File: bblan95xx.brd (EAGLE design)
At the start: 50 x 50 mm, 49 parts, among them IC1 LAN9512, IC2 93ST, Q1 25MHz

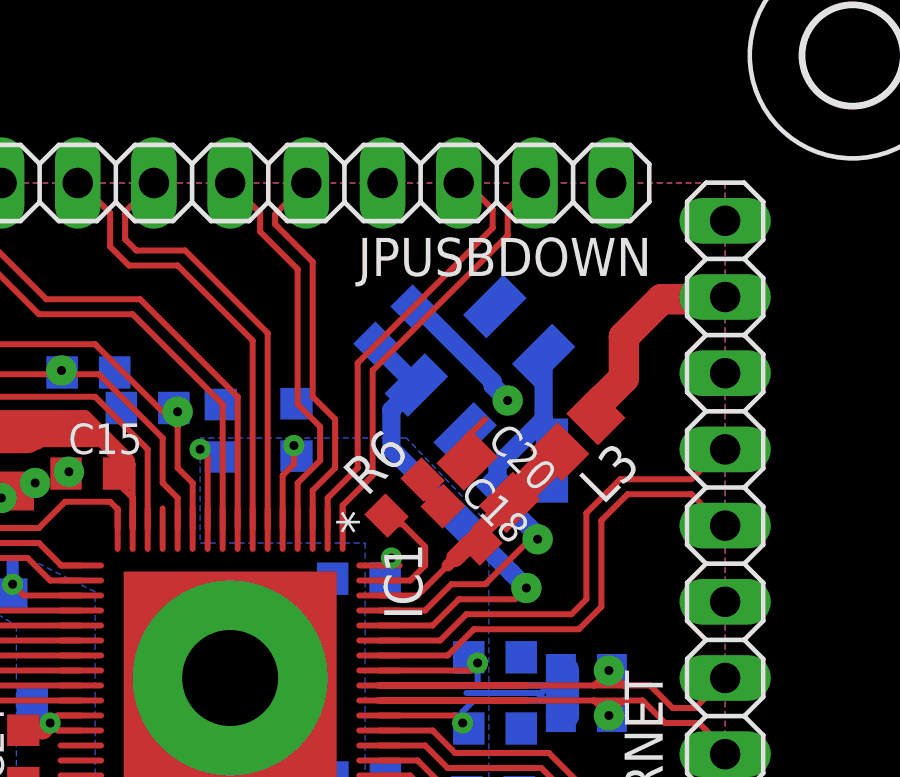
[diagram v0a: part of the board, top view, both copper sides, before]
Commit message: reroute USB down-port two and crystal cap
Signed-off-by: Stephan Baerwolf <stephan@matrixstorm.com>
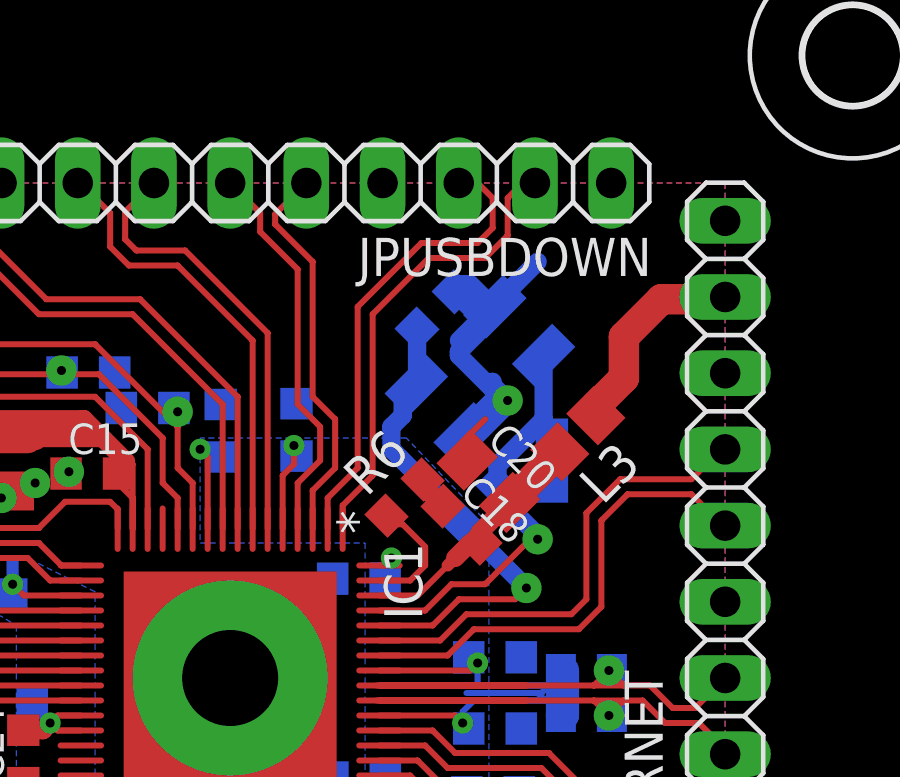
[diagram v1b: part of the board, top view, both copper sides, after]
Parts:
- moved C23 1.46 mm to (31.8, 37.3)
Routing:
- net GND: track 28.6 -> 37.0 mm
- net USBDP2: track 14.4 -> 15.7 mm
- net USBDM2: track 14.2 -> 15.5 mm
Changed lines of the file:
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@@
 <wire x1="29.375" y1="20.625" x2="20.625" y2="20.625" width="1.016" layer="41"/>
 <wire x1="20.625" y1="20.625" x2="20.625" y2="29.375" width="1.016" layer="41"/>
-<wire x1="28.5" y1="29.25" x2="28.5" y2="30.875" width="3" layer="41"/>
-<wire x1="28.5" y1="30.875" x2="29.5" y2="31.875" width="3" layer="41"/>
-<wire x1="29.5" y1="31.875" x2="29.5" y2="35.375" width="3" layer="41"/>
-<wire x1="29.5" y1="35.375" x2="33.875" y2="39.75" width="3" layer="41"/>
-<wire x1="33.875" y1="39.75" x2="33.875" y2="40.75" width="3" layer="41"/>
+<wire x1="28.5" y1="29.25" x2="28.5" y2="30.875" width="2.1844" layer="41"/>
+<wire x1="28.5" y1="30.875" x2="29.5" y2="31.875" width="2.1844" layer="41"/>
+<wire x1="29.5" y1="31.875" x2="29.5" y2="37.25" width="2.1844" layer="41"/>
 <wire x1="27.5" y1="29.25" x2="27.5" y2="31.375" width="3" layer="41"/>
 <wire x1="27.5" y1="31.375" x2="28.125" y2="32" width="3" layer="41"/>
@@
 <wire x1="21.25" y1="39.5" x2="21.25" y2="40.75" width="3" layer="41"/>
 <wire x1="25" y1="29.125" x2="25" y2="34.25" width="3" layer="41"/>
-<wire x1="25" y1="34.25" x2="21.875" y2="37.375" width="3" layer="41"/>
-<wire x1="21.875" y1="37.375" x2="18.75" y2="37.375" width="3" layer="41"/>
-<wire x1="18.75" y1="37.375" x2="16.125" y2="40" width="3" layer="41"/>
+<wire x1="25" y1="34.25" x2="21.875" y2="37.375" width="2.1844" layer="41"/>
+<wire x1="21.875" y1="37.375" x2="18.75" y2="37.375" width="2.1844" layer="41"/>
+<wire x1="18.75" y1="37.375" x2="16.125" y2="40" width="2.1844" layer="41"/>
 <wire x1="16.125" y1="40" x2="16.125" y2="40.75" width="3" layer="41"/>
 <wire x1="29.125" y1="26" x2="32.125" y2="26" width="3" layer="41"/>
@@
 <wire x1="39.875" y1="16.125" x2="41.25" y2="16.125" width="3" layer="41"/>
 <wire x1="40.25" y1="17" x2="40.25" y2="15.25" width="3" layer="41"/>
+<wire x1="29.5" y1="37.25" x2="31.5" y2="39.25" width="2.1844" layer="41"/>
+<wire x1="31.5" y1="39.25" x2="33.375" y2="39.25" width="2.1844" layer="41"/>
+<wire x1="33.375" y1="39.25" x2="34" y2="39.875" width="2.1844" layer="41"/>
+<wire x1="34" y1="39.875" x2="34" y2="41" width="3" layer="41"/>
 </plain>
 <attributes>
@@
 <attribute name="NAME" x="16.73" y="23.51" size="1.016" layer="26" rot="MR180"/>
 </element>
-<element name="C23" library="resistor" package="C0603K" value="33p" x="30.473765625" y="36.752046875" rot="MR315">
-<attribute name="SPICEPREFIX" value="C" x="30.473765625" y="36.752046875" size="1.778" layer="28" rot="MR315" display="off"/>
+<element name="C23" library="resistor" package="C0603K" value="33p" x="31.848765625" y="37.252046875" rot="MR315">
+<attribute name="SPICEPREFIX" value="C" x="31.848765625" y="37.252046875" size="1.778" layer="28" rot="MR315" display="off"/>
 </element>
 <element name="C24" library="resistor" package="C0603K" value=".1u" x="18.105" y="22.385" smashed="yes" rot="R90">
@@
 <vertex x="8.5" y="8.5"/>
 </polygon>
-<wire x1="31.092484375" y1="37.3707625" x2="31.2542375" y2="37.3707625" width="0.6096" layer="16"/>
 <wire x1="31.414678125" y1="31.61518125" x2="31.414678125" y2="31.40854375" width="0.6096" layer="1"/>
 <wire x1="31.414678125" y1="31.40854375" x2="32.094671875" y2="30.72855" width="0.6096" layer="1"/>
-<wire x1="31.2542375" y1="37.3707625" x2="33.75" y2="34.875" width="0.6096" layer="16"/>
 <wire x1="33.75" y1="34.875" x2="33.75" y2="34.75" width="0.6096" layer="16"/>
-<wire x1="33.75" y1="34.75" x2="34.25" y2="34.25" width="0.6096" layer="16"/>
+<wire x1="33.75" y1="34.75" x2="34" y2="34.5" width="0.6096" layer="16"/>
 <contactref element="C19" pad="1"/>
+<wire x1="34" y1="34.5" x2="34.25" y2="34.25" width="0.6096" layer="16"/>
 <wire x1="31.720228125" y1="18.428496875" x2="32.351359375" y2="18.428496875" width="1.016" layer="1"/>
 <wire x1="32.351359375" y1="18.428496875" x2="33.170725" y2="17.60913125" width="1.016" layer="1"/>
@@
 <wire x1="32.900215625" y1="32.264928125" x2="32.900215625" y2="33.025215625" width="0.2" layer="1"/>
 <wire x1="32.900215625" y1="33.025215625" x2="33.5" y2="33.625" width="0.2" layer="1"/>
+<wire x1="32.467484375" y1="37.8707625" x2="33.5" y2="36.838246875" width="0.6096" layer="16"/>
+<wire x1="33.5" y1="36.838246875" x2="33.5" y2="36.75" width="0.6096" layer="16"/>
+<wire x1="33.5" y1="36.75" x2="32.625" y2="35.875" width="0.6096" layer="16"/>
+<wire x1="32.625" y1="35.875" x2="32.625" y2="35.75" width="0.6096" layer="16"/>
+<wire x1="32.625" y1="35.75" x2="34.25" y2="34.125" width="0.6096" layer="16"/>
+<wire x1="34.25" y1="34.125" x2="33" y2="32.875" width="0.6096" layer="16"/>
+<wire x1="33.25" y1="33.75" x2="34" y2="34.5" width="0.6096" layer="16"/>
+<wire x1="35.25" y1="38.875" x2="34.125" y2="37.75" width="0.6096" layer="16"/>
+<wire x1="33" y1="38.125" x2="33.5" y2="37.625" width="0.6096" layer="16"/>
+<wire x1="33" y1="38.125" x2="32.721721875" y2="38.125" width="0.6096" layer="16"/>
+<wire x1="32.721721875" y1="38.125" x2="32.467484375" y2="37.8707625" width="0.6096" layer="16"/>
+<wire x1="32.625" y1="36.25" x2="33.375" y2="37" width="0.6096" layer="16"/>
 </signal>
 <signal name="VDD18CORE">
@@
 <contactref element="C23" pad="2"/>
 <contactref element="Q1" pad="1"/>
-<wire x1="29.85505" y1="36.133328125" x2="29.85505" y2="36.1157875" width="0.6096" layer="16"/>
-<wire x1="29.85505" y1="36.1157875" x2="31.20669375" y2="34.76414375" width="0.6096" layer="16"/>
-<wire x1="31.20669375" y1="34.76414375" x2="30.375" y2="33.93245" width="0.6096" layer="16"/>
-<wire x1="30.375" y1="33.93245" x2="30.375" y2="32.625" width="0.6096" layer="16"/>
 <wire x1="30.375" y1="32.625" x2="32.70859375" y2="30.29140625" width="0.6096" layer="16"/>
 <wire x1="32.70859375" y1="30.29140625" x2="32.70859375" y2="30.178265625" width="0.6096" layer="16"/>
 <wire x1="32.70859375" y1="30.178265625" x2="32.70859375" y2="29.66640625" width="0.2" layer="16"/>
 <via x="34.875" y="28" extent="1-16" drill="0.3" diameter="1.016" shape="octagon"/>
-<wire x1="34.375" y1="28.511859375" x2="34.130928125" y2="28.75593125" width="0.6096" layer="16"/>
 <contactref element="IC1" pad="60"/>
-<wire x1="34.130928125" y1="28.75593125" x2="32.70859375" y2="30.178265625" width="0.6096" layer="16"/>
+<wire x1="34.875" y1="28.011859375" x2="32.70859375" y2="30.178265625" width="0.6096" layer="16"/>
 <wire x1="29.977" y1="26.75" x2="31.75" y2="26.75" width="0.2" layer="1"/>
 <wire x1="31.75" y1="26.75" x2="32.625" y2="27.625" width="0.2" layer="1"/>
@@
 <wire x1="34.5" y1="27.625" x2="34.875" y2="28" width="0.2" layer="1"/>
 <wire x1="34.875" y1="28" x2="34.875" y2="28.011859375" width="0.6096" layer="16"/>
-<wire x1="34.875" y1="28.011859375" x2="34.375" y2="28.511859375" width="0.6096" layer="16"/>
+<wire x1="31.20669375" y1="34.76414375" x2="31.23005" y2="34.7875" width="0.6096" layer="16"/>
+<wire x1="31.23005" y1="34.7875" x2="31.23005" y2="36.633328125" width="0.6096" layer="16"/>
+<wire x1="30.375" y1="32.625" x2="30.375" y2="33.375" width="0.6096" layer="16"/>
+<wire x1="30.375" y1="33.375" x2="30.75" y2="33.75" width="0.6096" layer="16"/>
+<wire x1="30.75" y1="33.75" x2="30.75" y2="34.30745" width="0.6096" layer="16"/>
+<wire x1="30.75" y1="34.30745" x2="31.20669375" y2="34.76414375" width="0.6096" layer="16"/>
 </signal>
 <signal name="EECS">
@@
 <wire x1="28.75" y1="29.977" x2="28.75" y2="30.75" width="0.2" layer="1"/>
 <wire x1="28.75" y1="30.75" x2="29.75" y2="31.75" width="0.2" layer="1"/>
-<wire x1="29.75" y1="31.75" x2="29.75" y2="35.25" width="0.2" layer="1"/>
-<wire x1="29.75" y1="35.25" x2="34.25" y2="39.75" width="0.2" layer="1"/>
-<wire x1="34.25" y1="39.75" x2="34.25" y2="40.625" width="0.2" layer="1"/>
-<wire x1="34.25" y1="40.625" x2="34.75" y2="41.125" width="0.2" layer="1"/>
-<wire x1="35.16" y1="41.5" x2="34.785" y2="41.125" width="0.2" layer="1"/>
-<wire x1="34.785" y1="41.125" x2="34.75" y2="41.125" width="0.2" layer="1"/>
+<wire x1="29.75" y1="31.75" x2="29.75" y2="37.125" width="0.2" layer="1"/>
+<wire x1="29.75" y1="37.125" x2="31.625" y2="39" width="0.2" layer="1"/>
+<wire x1="31.625" y1="39" x2="33.5" y2="39" width="0.2" layer="1"/>
+<wire x1="33.5" y1="39" x2="34.25" y2="39.75" width="0.2" layer="1"/>
+<wire x1="34.25" y1="41" x2="34.25" y2="39.75" width="0.2" layer="1"/>
+<wire x1="34.25" y1="41" x2="34.75" y2="41.5" width="0.2" layer="1"/>
+<wire x1="34.75" y1="41.5" x2="35.16" y2="41.5" width="0.2" layer="1"/>
 </signal>
 <signal name="USBDP2">
@@
 <wire x1="28.25" y1="29.977" x2="28.25" y2="31" width="0.2" layer="1"/>
 <wire x1="28.25" y1="31" x2="29.25" y2="32" width="0.2" layer="1"/>
-<wire x1="29.25" y1="32" x2="29.25" y2="35.5" width="0.2" layer="1"/>
-<wire x1="29.25" y1="35.5" x2="33.75" y2="40" width="0.2" layer="1"/>
-<wire x1="33.75" y1="40.625" x2="33.75" y2="40" width="0.2" layer="1"/>
-<wire x1="33.75" y1="40.625" x2="33.25" y2="41.125" width="0.2" layer="1"/>
-<wire x1="32.62" y1="41.5" x2="32.995" y2="41.125" width="0.2" layer="1"/>
-<wire x1="32.995" y1="41.125" x2="33.25" y2="41.125" width="0.2" layer="1"/>
+<wire x1="29.25" y1="37.375" x2="29.25" y2="32" width="0.2" layer="1"/>
+<wire x1="29.25" y1="37.375" x2="31.375" y2="39.5" width="0.2" layer="1"/>
+<wire x1="31.375" y1="39.5" x2="33.25" y2="39.5" width="0.2" layer="1"/>
+<wire x1="33.25" y1="39.5" x2="33.75" y2="40" width="0.2" layer="1"/>
+<wire x1="33.75" y1="40" x2="33.75" y2="41" width="0.2" layer="1"/>
+<wire x1="33.75" y1="41" x2="33.25" y2="41.5" width="0.2" layer="1"/>
+<wire x1="33.25" y1="41.5" x2="32.62" y2="41.5" width="0.2" layer="1"/>
 </signal>
 <signal name="USBDM3">

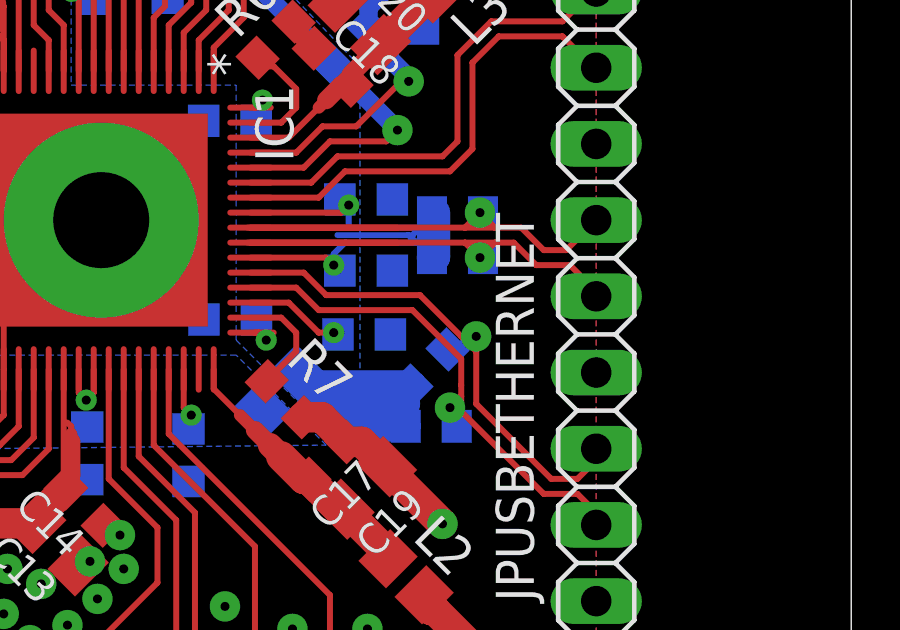
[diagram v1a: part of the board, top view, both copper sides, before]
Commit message: add extra analog capacitor and route VDD33A to free PIN
Signed-off-by: Stephan Baerwolf <stephan@matrixstorm.com>
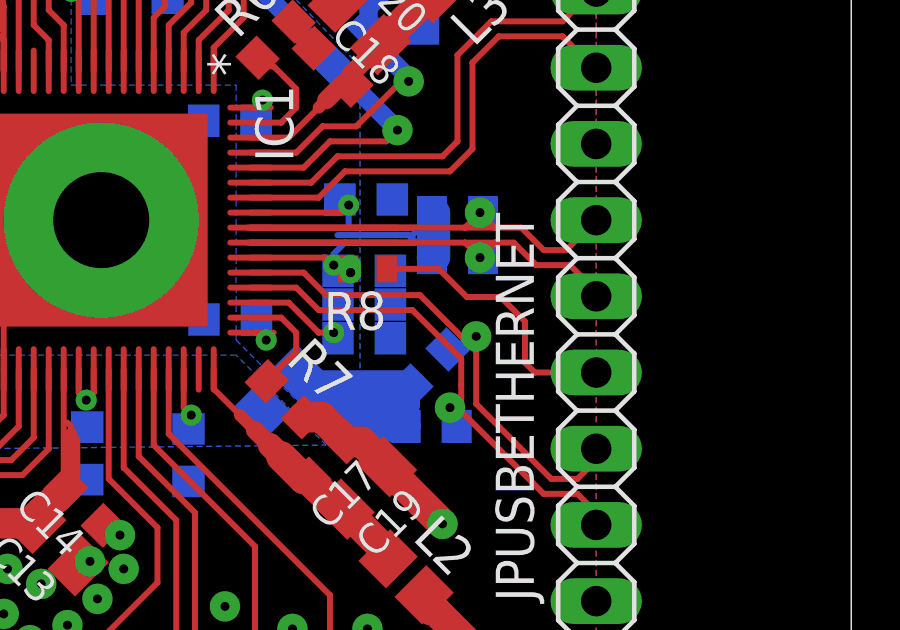
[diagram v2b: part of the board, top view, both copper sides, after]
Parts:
- added C29: .1u, resistor:C0603K
- added R8: (no value), resistor:R0402
- moved C9 0.12 mm to (33.8, 21.1)
- moved C10 0.06 mm to (33.8, 23.3)
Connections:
- new net VBIAS: JPUSBETHERNET.5, R8.1
- net GND: now also C29.1
- net VDD33A: now also C29.2, R8.2
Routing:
- net VBIAS: track 0.00 -> 9.21 mm
- net VDD33A: track 40.1 -> 40.3 mm, vias 7 -> 10
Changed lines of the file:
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@@
 <attribute name="NAME" x="16.045" y="27.135" size="1.016" layer="26" rot="MR180"/>
 </element>
-<element name="C10" library="resistor" package="C0603K" value=".1u" x="33.83" y="23.315" smashed="yes" rot="MR0">
-<attribute name="SPICEPREFIX" value="C" x="33.83" y="23.315" size="1.778" layer="28" rot="MR0" display="off"/>
-<attribute name="NAME" x="34.63" y="23.965" size="1.016" layer="26" rot="MR0"/>
+<element name="C10" library="resistor" package="C0603K" value=".1u" x="33.765" y="23.315" smashed="yes" rot="MR0">
+<attribute name="SPICEPREFIX" value="C" x="33.765" y="23.315" size="1.778" layer="28" rot="MR0" display="off"/>
+<attribute name="NAME" x="34.565" y="23.965" size="1.016" layer="26" rot="MR0"/>
 </element>
 <element name="C11" library="resistor" package="C0603K" value=".1u" x="33.83" y="25.69" smashed="yes" rot="MR0">
@@
 <attribute name="NAME" x="28.5" y="21.035" size="1.016" layer="26" rot="MR180"/>
 </element>
-<element name="C9" library="resistor" package="C0603K" value=".1u" x="33.765" y="21.19" smashed="yes" rot="MR0">
-<attribute name="SPICEPREFIX" value="C" x="33.765" y="21.19" size="1.778" layer="28" rot="MR0" display="off"/>
-<attribute name="NAME" x="34.565" y="21.84" size="1.016" layer="26" rot="MR0"/>
+<element name="C9" library="resistor" package="C0603K" value=".1u" x="33.765" y="21.065" smashed="yes" rot="MR0">
+<attribute name="SPICEPREFIX" value="C" x="33.765" y="21.065" size="1.778" layer="28" rot="MR0" display="off"/>
+<attribute name="NAME" x="34.565" y="21.715" size="1.016" layer="26" rot="MR0"/>
 </element>
 <element name="IC1" library="LAN95XX" package="QFN64-9X9-EXTRALONG" value="LAN9512" x="25" y="25" rot="R270"/>
@@
 </element>
 <element name="L1" library="resistor" package="R0805" value="120Rat100MHz" x="30.97423125" y="19.271215625" smashed="yes" rot="MR315">
+<attribute name="NAME" x="30.794628125" y="20.528453125" size="1.27" layer="26" rot="MR315"/>
 <attribute name="SPICEPREFIX" value="R" x="30.97423125" y="19.271215625" size="1.778" layer="28" rot="MR315" display="off"/>
-<attribute name="NAME" x="30.794628125" y="20.528453125" size="1.27" layer="26" rot="MR315"/>
 </element>
 <element name="L2" library="resistor" package="R0805" value="120Rat100MHz" x="35.16365625" y="13.11235" rot="R315">
@@
 <element name="R1" library="resistor" package="R0603" value="" x="36.875" y="25.25" rot="MR0">
 <attribute name="SPICEPREFIX" value="R" x="36.875" y="25.25" size="1.778" layer="28" rot="MR0" display="off"/>
+</element>
+<element name="C29" library="resistor" package="C0603K" value=".1u" x="33.765" y="22.1875" rot="MR0">
+<attribute name="SPICEPREFIX" value="C" x="33.765" y="22.1875" size="1.778" layer="28" rot="MR0" display="off"/>
+</element>
+<element name="R8" library="resistor" package="R0402" value="" x="33.875" y="23.375" rot="R180">
+<attribute name="SPICEPREFIX" value="R" x="33.875" y="23.375" size="1.778" layer="27" rot="R180" display="off"/>
 </element>
 </elements>
@@
 <wire x1="32.54111875" y1="18.9064125" x2="35.0935875" y2="18.9064125" width="1.016" layer="16"/>
 <wire x1="35.0935875" y1="18.9064125" x2="35.125" y2="18.875" width="1.016" layer="16"/>
+<contactref element="C29" pad="2"/>
+<contactref element="R8" pad="2"/>
+<via x="33.3125" y="23.25" extent="1-16" drill="0.3" shape="square"/>
+<via x="33.3125" y="23.5" extent="1-16" drill="0.001" diameter="0.7" shape="square"/>
+<via x="33.3125" y="23.25" extent="1-16" drill="0.3" shape="square"/>
+<wire x1="33.225" y1="23.375" x2="33.3125" y2="23.375" width="0.2" layer="1"/>
+<wire x1="33.3125" y1="23.375" x2="33.3125" y2="23.5" width="0.2" layer="1"/>
 </signal>
 <signal name="GND">
@@
 <wire x1="32.721721875" y1="38.125" x2="32.467484375" y2="37.8707625" width="0.6096" layer="16"/>
 <wire x1="32.625" y1="36.25" x2="33.375" y2="37" width="0.6096" layer="16"/>
+<contactref element="C29" pad="1"/>
 </signal>
 <signal name="VDD18CORE">
@@
 <wire x1="40.5" y1="24" x2="41.5" y2="25" width="0.2" layer="1"/>
 </signal>
+<signal name="VBIAS">
+<contactref element="R8" pad="1"/>
+<contactref element="JPUSBETHERNET" pad="5"/>
+<wire x1="34.525" y1="23.375" x2="36.25" y2="23.375" width="0.2" layer="1"/>
+<wire x1="41.5" y1="19.92" x2="39.455" y2="19.92" width="0.2" layer="1"/>
+<wire x1="39.455" y1="19.92" x2="39.125" y2="20.25" width="0.2" layer="1"/>
+<wire x1="39.125" y1="20.25" x2="39.125" y2="21.625" width="0.2" layer="1"/>
+<wire x1="36.25" y1="23.375" x2="37.1875" y2="22.4375" width="0.2" layer="1"/>
+<wire x1="37.1875" y1="22.4375" x2="38.3125" y2="22.4375" width="0.2" layer="1"/>
+<wire x1="38.3125" y1="22.4375" x2="39.125" y2="21.625" width="0.2" layer="1"/>
+</signal>
+<signal name="N$2">
+<wire x1="34.5" y1="23.625" x2="34.375" y2="23.625" width="0.2" layer="1"/>
+<wire x1="34.375" y1="23.625" x2="34.375" y2="23.5" width="0.2" layer="1"/>
+</signal>
 </signals>
